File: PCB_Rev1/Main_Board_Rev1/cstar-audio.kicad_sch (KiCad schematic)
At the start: 2 parts, among them J12 532610771, J13 532610771

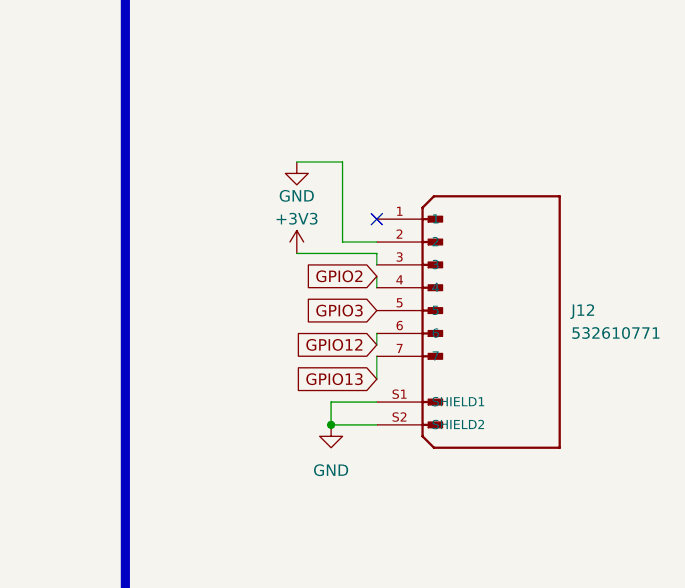
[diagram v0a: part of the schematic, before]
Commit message: Audio Connector Pins
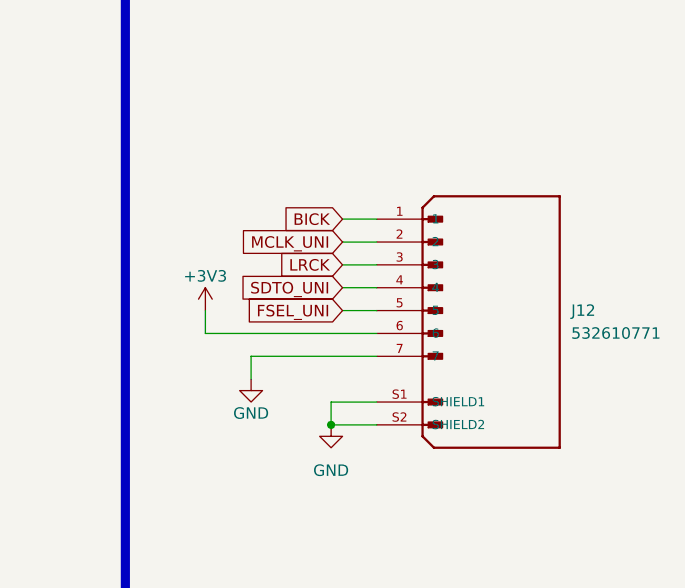
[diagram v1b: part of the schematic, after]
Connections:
- net GPIO12 is gone; now on net +3V3: J12.6
- net GPIO13 is gone; now on net GND: J12.7
- net +3V3: no longer J12.3
- net GND: no longer J12.2
- net BICK: now reaches J12.1
- net GPIO2 renamed SDTO_UNI
- net GPIO3 renamed FSEL_UNI
- new net LRCK: J12.3
- new net MCLK_UNI: J12.2
- no-connect marks 2 -> 1
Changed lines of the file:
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@@
 		(at 198.12 95.25)
 	)
-	(no_connect
-		(at 78.74 95.25)
-	)
 	(wire
 		(pts
@@
 	(wire
 		(pts
+			(xy 78.74 110.49) (xy 64.77 110.49)
+		)
+		(stroke
+			(width 0)
+			(type default)
+		)
+	)
+	(wire
+		(pts
+			(xy 59.69 107.95) (xy 78.74 107.95)
+		)
+		(stroke
+			(width 0)
+			(type default)
+		)
+	)
+	(wire
+		(pts
 			(xy 78.74 115.57) (xy 73.66 115.57)
 		)
@@
 	(wire
 		(pts
+			(xy 64.77 110.49) (xy 64.77 113.03)
+		)
+		(stroke
+			(width 0)
+			(type default)
+		)
+	)
+	(wire
+		(pts
 			(xy 194.31 97.79) (xy 194.31 88.9)
 		)
@@
 	(wire
 		(pts
+			(xy 74.93 102.87) (xy 78.74 102.87)
+		)
+		(stroke
+			(width 0)
+			(type default)
+		)
+	)
+	(wire
+		(pts
 			(xy 194.31 88.9) (xy 189.23 88.9)
 		)
@@
 	(wire
 		(pts
-			(xy 78.74 99.06) (xy 78.74 100.33)
-		)
-		(stroke
-			(width 0)
-			(type default)
-		)
-	)
-	(wire
-		(pts
-			(xy 69.85 99.06) (xy 78.74 99.06)
+			(xy 74.93 97.79) (xy 78.74 97.79)
 		)
 		(stroke
@@
 	(wire
 		(pts
-			(xy 78.74 113.03) (xy 78.74 110.49)
-		)
-		(stroke
-			(width 0)
-			(type default)
-		)
-	)
-	(wire
-		(pts
 			(xy 198.12 113.03) (xy 198.12 110.49)
 		)
@@
 	(wire
 		(pts
-			(xy 78.74 97.79) (xy 74.93 97.79)
-		)
-		(stroke
-			(width 0)
-			(type default)
-		)
-	)
-	(wire
-		(pts
 			(xy 189.23 99.06) (xy 198.12 99.06)
 		)
@@
 	(wire
 		(pts
+			(xy 74.93 105.41) (xy 78.74 105.41)
+		)
+		(stroke
+			(width 0)
+			(type default)
+		)
+	)
+	(wire
+		(pts
 			(xy 193.04 118.11) (xy 198.12 118.11)
 		)
@@
 	(wire
 		(pts
-			(xy 74.93 88.9) (xy 69.85 88.9)
+			(xy 59.69 105.41) (xy 59.69 107.95)
 		)
 		(stroke
@@
 	(wire
 		(pts
+			(xy 74.93 100.33) (xy 78.74 100.33)
+		)
+		(stroke
+			(width 0)
+			(type default)
+		)
+	)
+	(wire
+		(pts
 			(xy 198.12 109.22) (xy 198.12 107.95)
 		)
@@
 	(wire
 		(pts
-			(xy 78.74 109.22) (xy 78.74 107.95)
-		)
-		(stroke
-			(width 0)
-			(type default)
-		)
-	)
-	(wire
-		(pts
-			(xy 78.74 101.6) (xy 78.74 102.87)
-		)
-		(stroke
-			(width 0)
-			(type default)
-		)
-	)
-	(wire
-		(pts
-			(xy 74.93 97.79) (xy 74.93 88.9)
+			(xy 74.93 95.25) (xy 78.74 95.25)
 		)
 		(stroke
@@
 		)
 	)
-	(global_label "GPIO13"
+	(global_label "FSEL_UNI"
 		(shape input)
-		(at 78.74 113.03 180)
+		(at 74.93 105.41 180)
+		(fields_autoplaced yes)
+		(effects
+			(font
+				(size 1.27 1.27)
+			)
+			(justify right)
+		)
+		(property "Intersheetrefs" "${INTERSHEET_REFS}"
+			(at 63.2362 105.41 0)
+			(effects
+				(font
+					(size 1.27 1.27)
+				)
+				(justify right)
+				(hide yes)
+			)
+		)
+	)
+	(global_label "BICK"
+		(shape input)
+		(at 74.93 95.25 180)
 		(fields_autoplaced yes)
 		(effects
@@
 		)
 		(property "Intersheetrefs" "${INTERSHEET_REFS}"
-			(at 68.3845 113.03 0)
+			(at 67.53 95.25 0)
 			(effects
 				(font
@@
 		)
 	)
-	(global_label "GPIO3"
+	(global_label "LRCK"
 		(shape input)
-		(at 78.74 105.41 180)
+		(at 74.93 100.33 180)
 		(fields_autoplaced yes)
 		(effects
@@
 		)
 		(property "Intersheetrefs" "${INTERSHEET_REFS}"
-			(at 69.594 105.41 0)
+			(at 67.1067 100.33 0)
 			(effects
 				(font
@@
 		)
 	)
-	(global_label "GPIO2"
+	(global_label "SDTO_UNI"
 		(shape input)
-		(at 78.74 101.6 180)
+		(at 74.93 102.87 180)
 		(fields_autoplaced yes)
 		(effects
@@
 		)
 		(property "Intersheetrefs" "${INTERSHEET_REFS}"
-			(at 69.594 101.6 0)
+			(at 62.9338 102.87 0)
 			(effects
 				(font
@@
 		)
 	)
-	(global_label "GPIO12"
+	(global_label "MCLK_UNI"
 		(shape input)
-		(at 78.74 109.22 180)
+		(at 74.93 97.79 180)
 		(fields_autoplaced yes)
 		(effects
@@
 		)
 		(property "Intersheetrefs" "${INTERSHEET_REFS}"
-			(at 68.3845 109.22 0)
+			(at 62.6919 97.79 0)
 			(effects
 				(font
@@
 	(symbol
 		(lib_id "power:GND")
-		(at 69.85 88.9 0)
+		(at 64.77 113.03 0)
+		(mirror y)
 		(unit 1)
 		(exclude_from_sim no)
@@
 		(dnp no)
 		(property "Reference" "#PWR045"
-			(at 69.85 95.25 0)
+			(at 64.77 119.38 0)
 			(effects
 				(font
@@
 		)
 		(property "Value" "GND"
-			(at 69.85 92.71 0)
+			(at 64.77 116.84 0)
 			(effects
 				(font
@@
 		)
 		(property "Footprint" ""
-			(at 69.85 88.9 0)
+			(at 64.77 113.03 0)
 			(effects
 				(font
@@
 		)
 		(property "Datasheet" ""
-			(at 69.85 88.9 0)
+			(at 64.77 113.03 0)
 			(effects
 				(font
@@
 		)
 		(property "Description" ""
-			(at 69.85 88.9 0)
+			(at 64.77 113.03 0)
 			(effects
 				(font
@@
 	(symbol
 		(lib_id "power:+3V3")
-		(at 69.85 99.06 0)
+		(at 59.69 105.41 0)
 		(unit 1)
 		(exclude_from_sim no)
@@
 		(dnp no)
 		(property "Reference" "#PWR048"
-			(at 69.85 102.87 0)
+			(at 59.69 109.22 0)
 			(effects
 				(font
@@
 		)
 		(property "Value" "+3V3"
-			(at 69.85 95.25 0)
+			(at 59.69 101.6 0)
 			(effects
 				(font
@@
 		)
 		(property "Footprint" ""
-			(at 69.85 99.06 0)
+			(at 59.69 105.41 0)
 			(effects
 				(font
@@
 		)
 		(property "Datasheet" ""
-			(at 69.85 99.06 0)
+			(at 59.69 105.41 0)
 			(effects
 				(font
@@
 		)
 		(property "Description" ""
-			(at 69.85 99.06 0)
-			(effects
-				(font
+			(at 59.69 105.41 0)
+			(effects
+				(font

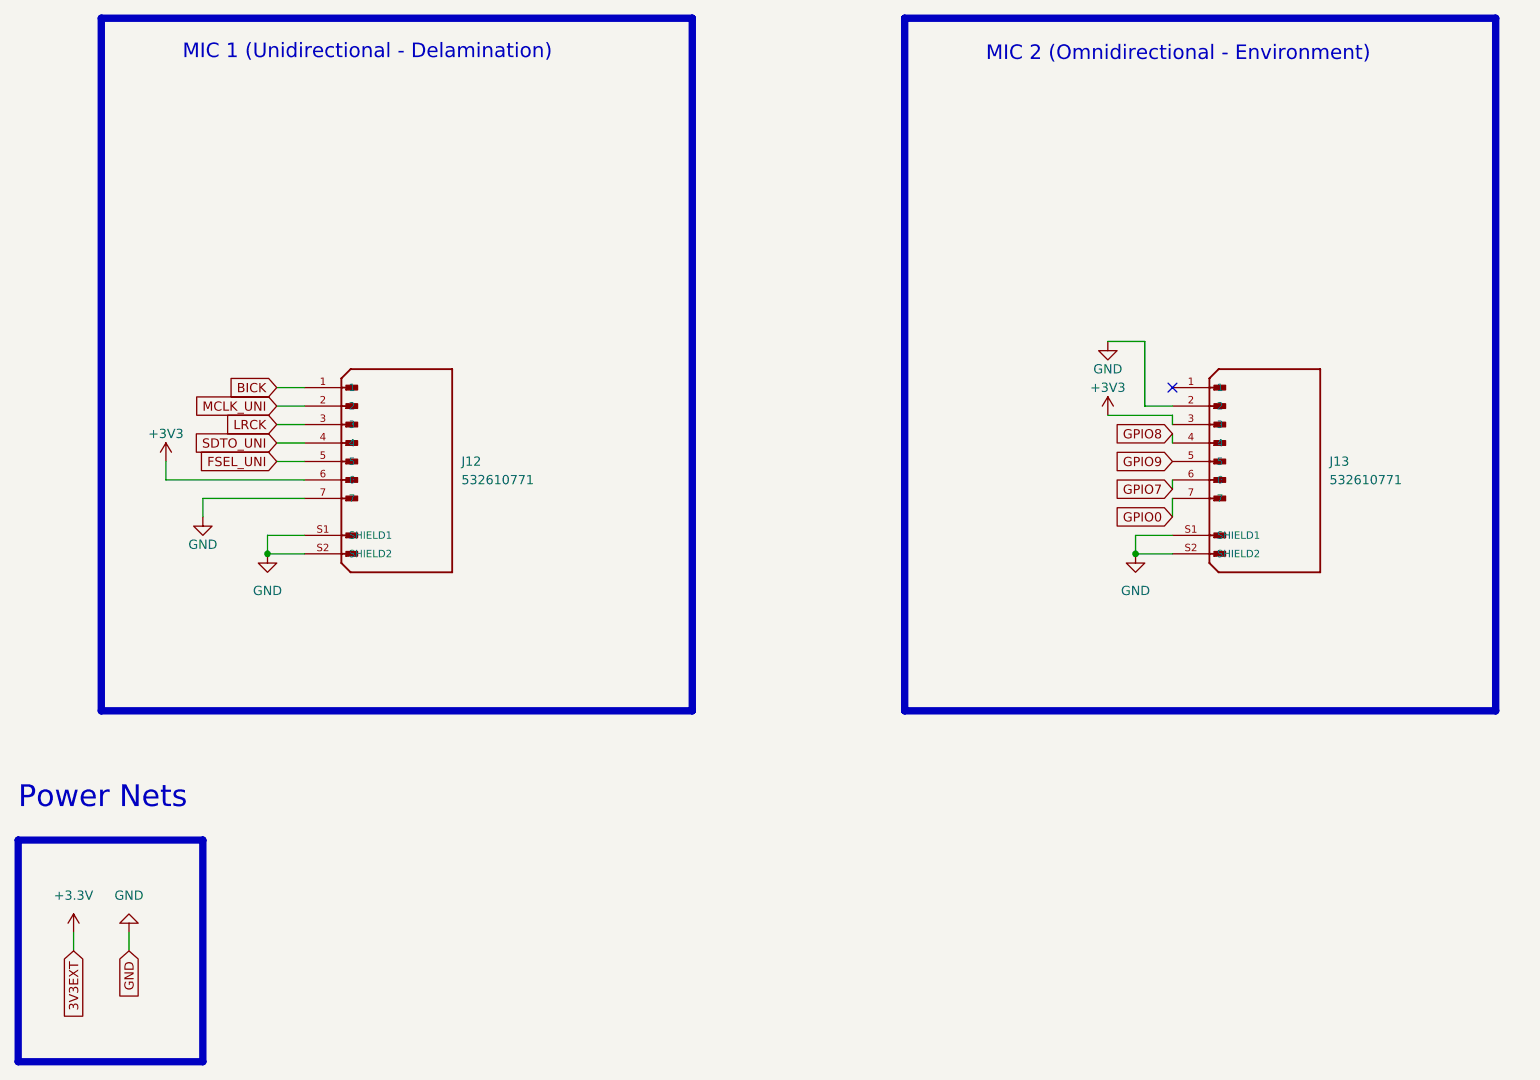
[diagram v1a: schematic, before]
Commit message: Connections Adjustments
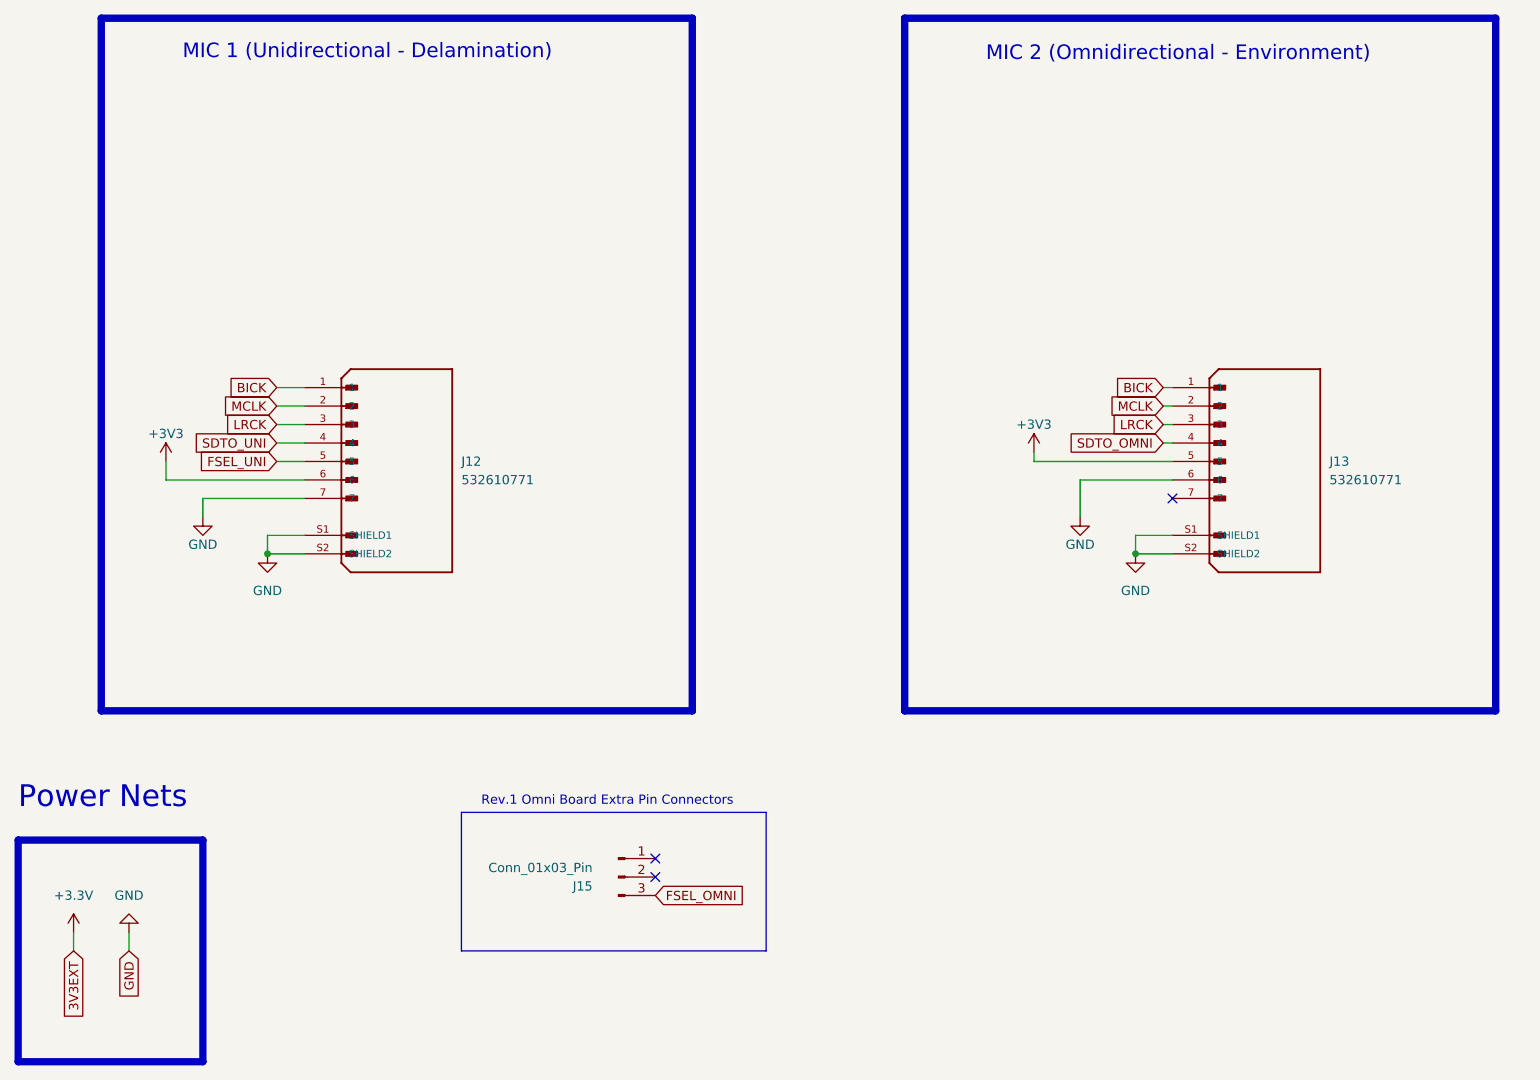
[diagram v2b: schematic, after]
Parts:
- added J15: Conn_01x03_Pin, Connector_PinHeader_2.54mm:PinHeader_1x03_P2.54mm_Vertical, symbol Connector:Conn_01x03_Pin
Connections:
- net GPIO7 is gone; now on net GND: J13.6
- net GPIO9 is gone; now on net +3V3: J13.5
- net +3V3: no longer J13.3
- net BICK: now also J13.1
- net GND: no longer J13.2
- net LRCK: now also J13.3
- net GPIO0: no longer names the net of J13.7
- net GPIO8 renamed SDTO_OMNI
- net MCLK_UNI renamed MCLK
- net MCLK: now also J13.2
- new net FSEL_OMNI: J15.3 (Pin_3)
- no-connect marks 1 -> 3
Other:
- note added: "Rev.1 Omni Board Extra Pin Connectors"

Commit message: Micboard Done with traces
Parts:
- removed J15: Conn_01x03_Pin, Connector_PinHeader_2.54mm:PinHeader_1x03_P2.54mm_Vertical, symbol Connector:Conn_01x03_Pin
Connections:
- net +3V3: now also J13.6; no longer J13.5
- net FSEL_OMNI: now also J13.5
- net GND: now also J13.7; no longer J13.6
- net MCLK: no longer J13.2
- net SDTO_OMNI: now also J13.2; no longer J13.4
- net SDTO_UNI: now also J13.4
- no-connect marks 3 -> 0
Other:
- note removed: "Rev.1 Omni Board Extra Pin Connectors"

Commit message: LCSC + CSV changes
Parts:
- J12, J13: LCSC (none) -> C505276
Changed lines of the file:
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@@
+			)
+		)
+		(property "LCSC" "C505276"
+			(at 210.82 105.41 0)
+			(effects
+				(font
+					(size 1.27 1.27)
+				)
+				(hide yes)
 			)
 		)
@@
 				(hide yes)
 			)
+		)
+		(property "LCSC" "C505276"
+			(at 91.44 105.41 0)
+			(effects
+				(font
+					(size 1.27 1.27)
+				)
+				(hide yes)
+			)
